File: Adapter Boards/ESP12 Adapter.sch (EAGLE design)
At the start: 3 parts, among them U1 WI07-12FULL

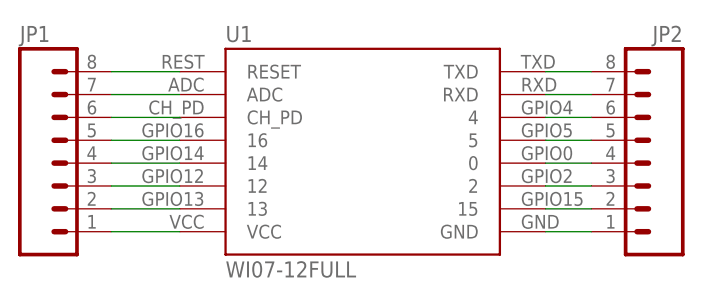
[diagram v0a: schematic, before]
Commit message: Repair pads; resize ESP12
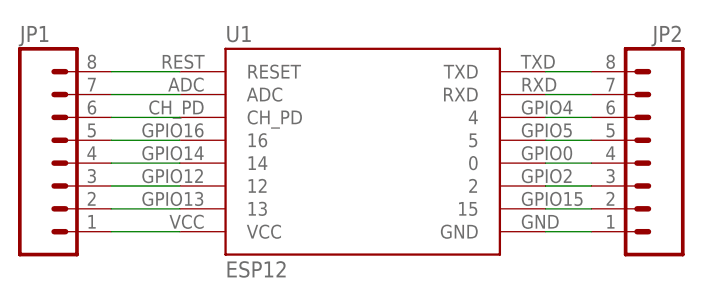
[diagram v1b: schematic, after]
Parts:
- U1: value WI07-12FULL -> ESP12; device ESP:WI07-12FULL -> ESP:ESP12
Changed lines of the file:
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@@
 <part name="JP1" library="SparkFun-Connectors" deviceset="M08" device=""/>
 <part name="JP2" library="SparkFun-Connectors" deviceset="M08" device=""/>
-<part name="U1" library="ESP" deviceset="WI07-12" device="FULL"/>
+<part name="U1" library="ESP" deviceset="ESP12" device=""/>
 </parts>
 <sheets>
